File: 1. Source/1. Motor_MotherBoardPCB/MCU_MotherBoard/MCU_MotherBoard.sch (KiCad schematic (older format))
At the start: 0 parts

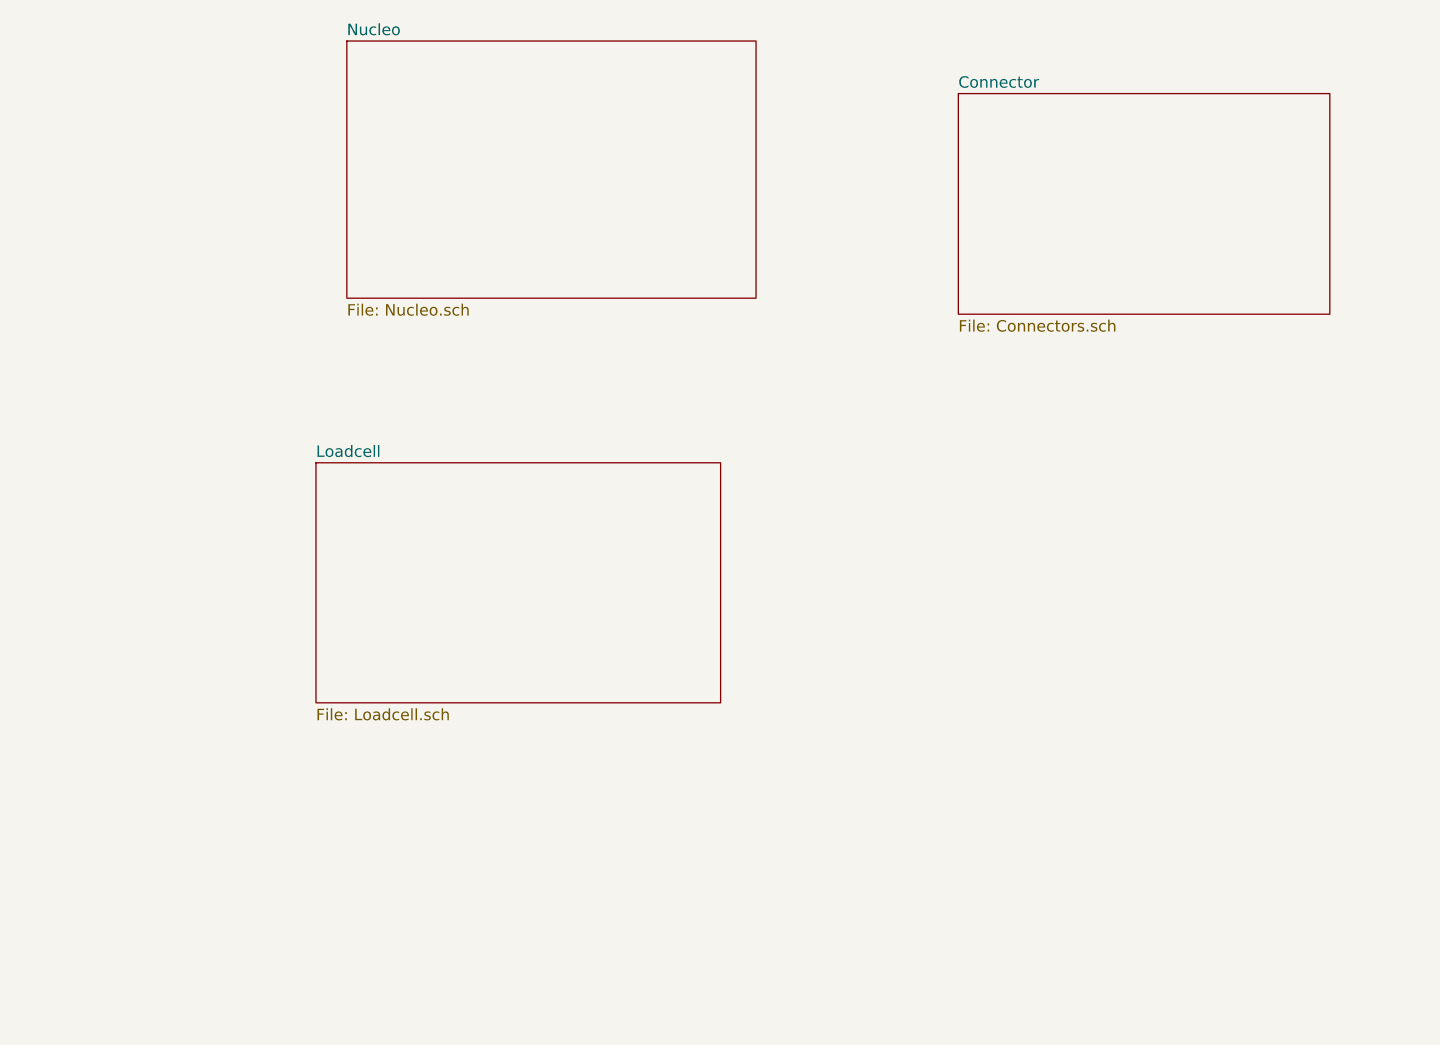
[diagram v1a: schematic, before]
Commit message: Add LoadCell_Click4 and SDCARD libraries
Add LoadCell_Click4 and SDCARD libraries
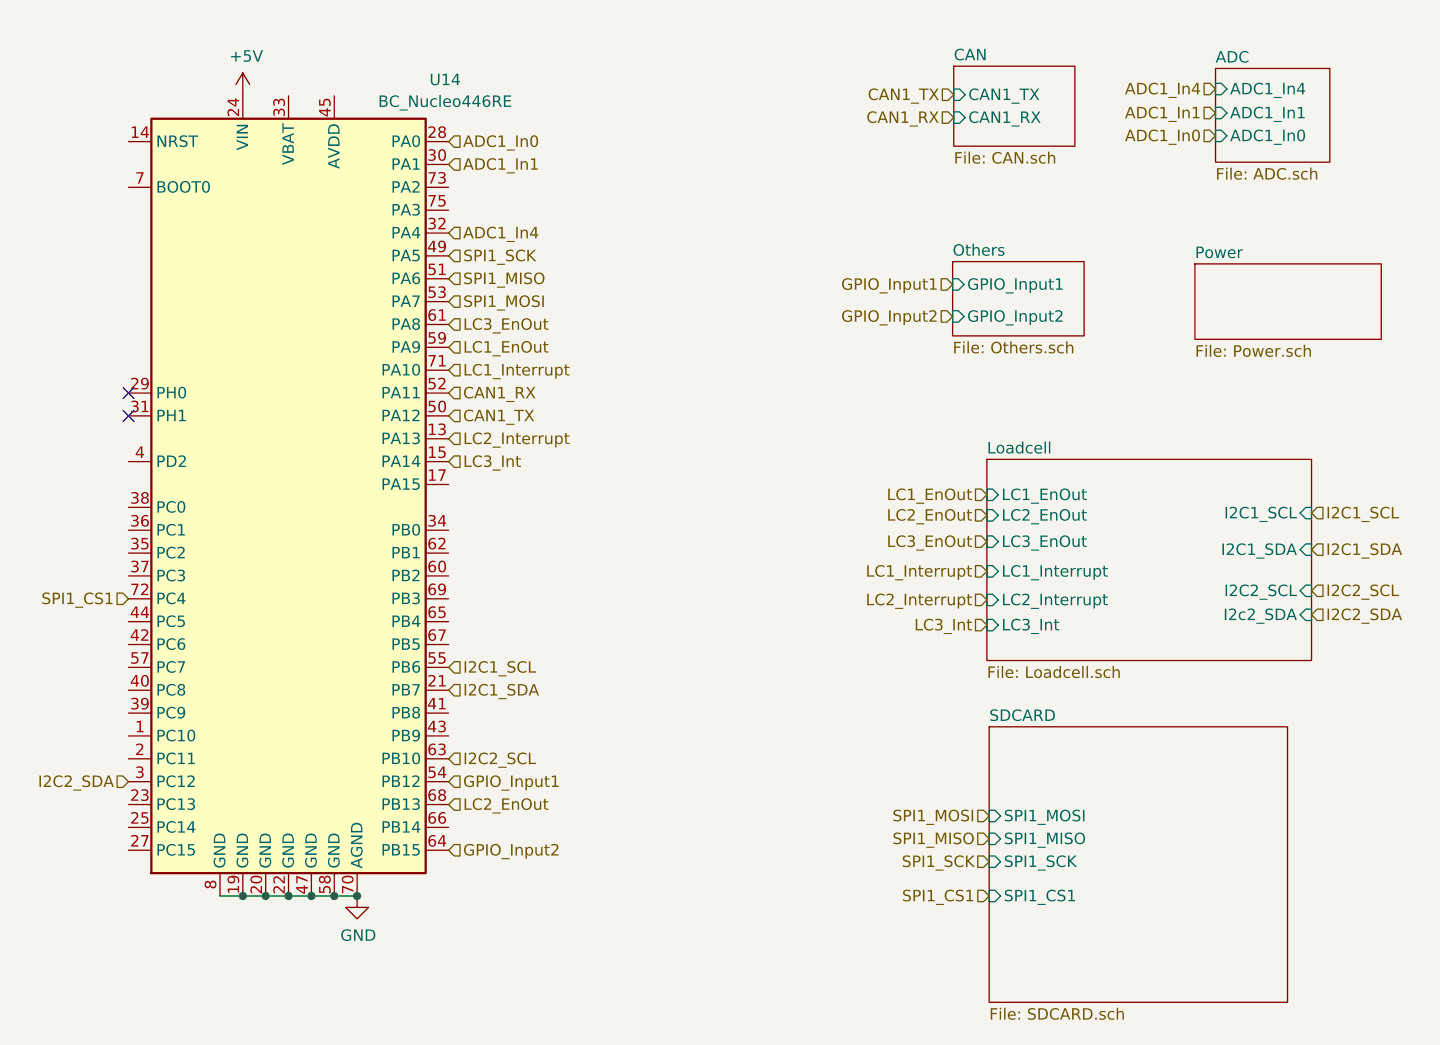
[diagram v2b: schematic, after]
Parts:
- added U14: BC_Nucleo446RE, BC_STM_Board:Main_NUCLEO-F446RE, symbol BC_Nucleo_boards:BC_Nucleo446RE
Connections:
- new net +5V: U14.24 (VIN)
- new net ADC1_In0: U14.28 (PA0)
- new net ADC1_In1: U14.30 (PA1)
- new net ADC1_In4: U14.32 (PA4)
- new net CAN1_RX: U14.52 (PA11)
- new net CAN1_TX: U14.50 (PA12)
- new net GND: U14.19 (GND), U14.20 (GND), U14.22 (GND), U14.47 (GND), U14.58 (GND), U14.70 (AGND), U14.8 (GND)
- new net GPIO_Input1: U14.54 (PB12)
- new net GPIO_Input2: U14.64 (PB15)
- new net I2C1_SCL: U14.55 (PB6)
- new net I2C1_SDA: U14.21 (PB7)
- new net I2C2_SCL: U14.63 (PB10)
- new net I2C2_SDA: U14.3 (PC12)
- new net LC1_EnOut: U14.59 (PA9)
- new net LC1_Interrupt: U14.71 (PA10)
- new net LC2_EnOut: U14.68 (PB13)
- new net LC2_Interrupt: U14.13 (PA13)
- new net LC3_EnOut: U14.61 (PA8)
- new net LC3_Int: U14.15 (PA14)
- new net SPI1_CS1: U14.72 (PC4)
- new net SPI1_MISO: U14.51 (PA6)
- new net SPI1_MOSI: U14.53 (PA7)
- new net SPI1_SCK: U14.49 (PA5)
- no-connect marks 0 -> 2
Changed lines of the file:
@@
 $Descr A4 11693 8268
 encoding utf-8
-Sheet 1 4
+Sheet 1 7
 Title ""
 Date ""
@@
 Comment4 ""
 $EndDescr
-$Sheet
-S 2095 1965 1790 1125
-U 6360BD6F
-F0 "Nucleo" 50
-F1 "Nucleo.sch" 50
-$EndSheet
-$Sheet
-S 4770 2195 1625 965
-U 6360BDB0
-F0 "Connector" 50
-F1 "Connectors.sch" 50
-$EndSheet
-$Sheet
-S 1960 3810 1770 1050
+$Comp
+L BC_Nucleo_boards:BC_Nucleo446RE U?
+U 1 1 63862899
+P 1840 3905
+AR Path="/6360BD6F/63862899" Ref="U?"  Part="1"
+AR Path="/63862899" Ref="U14"  Part="1"
+F 0 "U14" H 2525 5675 50  0000 C CNN
+F 1 "BC_Nucleo446RE" H 2525 5580 50  0000 C CNN
+F 2 "BC_STM_Board:Main_NUCLEO-F446RE" H 1240 2205 50  0001 R CNN
+F 3 "http://www.st.com/st-web-ui/static/active/en/resource/technical/document/datasheet/DM00141306.pdf" H 1840 3905 50  0001 C CNN
+	1    1840 3905
+	1    0    0    -1
+$EndComp
+Text HLabel 2540 4805 2    50   Input ~ 0
+I2C1_SDA
+Text HLabel 2540 4705 2    50   Input ~ 0
+I2C1_SCL
+NoConn ~ 1140 3505
+NoConn ~ 1140 3605
+Text HLabel 2540 3505 2    50   Input ~ 0
+CAN1_RX
+Text HLabel 2540 3605 2    50   Input ~ 0
+CAN1_TX
+Text HLabel 2540 5305 2    50   Input ~ 0
+LC2_EnOut
+Text HLabel 2540 3405 2    50   Input ~ 0
+LC1_Interrupt
+Wire Wire Line
+	1540 5705 1640 5705
+Connection ~ 1640 5705
+Wire Wire Line
+	1640 5705 1740 5705
+Connection ~ 1740 5705
+Wire Wire Line
+	1740 5705 1840 5705
+Connection ~ 1840 5705
+Wire Wire Line
+	1840 5705 1940 5705
+Connection ~ 1940 5705
+Wire Wire Line
+	1940 5705 2040 5705
+Connection ~ 2040 5705
+Wire Wire Line
+	2040 5705 2140 5705
+$Comp
+L power:GND #PWR?
+U 1 1 638628B2
+P 2140 5705
+AR Path="/6360BD6F/638628B2" Ref="#PWR?"  Part="1"
+AR Path="/638628B2" Ref="#PWR02"  Part="1"
+F 0 "#PWR02" H 2140 5455 50  0001 C CNN
+F 1 "GND" H 2145 5532 50  0000 C CNN
+F 2 "" H 2140 5705 50  0001 C CNN
+F 3 "" H 2140 5705 50  0001 C CNN
+	1    2140 5705
+	1    0    0    -1
+$EndComp
+Connection ~ 2140 5705
+$Comp
+L power:+5V #PWR?
+U 1 1 638628B9
+P 1640 2205
+AR Path="/6360BD6F/638628B9" Ref="#PWR?"  Part="1"
+AR Path="/638628B9" Ref="#PWR01"  Part="1"
+F 0 "#PWR01" H 1640 2055 50  0001 C CNN
+F 1 "+5V" H 1655 2378 50  0000 C CNN
+F 2 "" H 1640 2205 50  0001 C CNN
+F 3 "" H 1640 2205 50  0001 C CNN
+	1    1640 2205
+	1    0    0    -1
+$EndComp
+Text HLabel 2540 3305 2    50   Input ~ 0
+LC1_EnOut
+Text HLabel 2540 5105 2    50   Input ~ 0
+I2C2_SCL
+Text HLabel 2540 2905 2    50   Input ~ 0
+SPI1_SCK
+Text HLabel 2540 3005 2    50   Input ~ 0
+SPI1_MISO
+Text HLabel 2540 3105 2    50   Input ~ 0
+SPI1_MOSI
+Text HLabel 2540 5205 2    50   Input ~ 0
+GPIO_Input1
+Text HLabel 2540 5505 2    50   Input ~ 0
+GPIO_Input2
+Text HLabel 2540 2405 2    50   Input ~ 0
+ADC1_In0
+Text HLabel 2540 2805 2    50   Input ~ 0
+ADC1_In4
+Text HLabel 2540 2505 2    50   Input ~ 0
+ADC1_In1
+Text HLabel 1140 4405 0    50   Input ~ 0
+SPI1_CS1
+Text HLabel 1140 5205 0    50   Input ~ 0
+I2C2_SDA
+$Sheet
+S 4895 3795 1420 880
 U 6360BDDC
 F0 "Loadcell" 50
 F1 "Loadcell.sch" 50
-$EndSheet
+F2 "LC3_EnOut" I L 4895 4155 50
+F3 "LC2_EnOut" I L 4895 4040 50
+F4 "LC1_EnOut" I L 4895 3950 50
+F5 "LC1_Interrupt" I L 4895 4285 50
+F6 "LC2_Interrupt" I L 4895 4410 50
+F7 "LC3_Int" I L 4895 4520 50
+F8 "I2C1_SCL" I R 6315 4030 50
+F9 "I2C1_SDA" I R 6315 4190 50
+F10 "I2C2_SCL" I R 6315 4370 50
+F11 "I2c2_SDA" I R 6315 4475 50
+$EndSheet
+$Sheet
+S 4745 2930 575  325
+U 6360BDB0
+F0 "Others" 50
+F1 "Others.sch" 50
+F2 "GPIO_Input1" I L 4745 3030 50
+F3 "GPIO_Input2" I L 4745 3170 50
+$EndSheet
+Text HLabel 2540 3705 2    50   Input ~ 0
+LC2_Interrupt
+Text HLabel 2540 3805 2    50   Input ~ 0
+LC3_Int
+Text HLabel 2540 3205 2    50   Input ~ 0
+LC3_EnOut
+Text HLabel 4895 4155 0    50   Input ~ 0
+LC3_EnOut
+Text HLabel 4895 4040 0    50   Input ~ 0
+LC2_EnOut
+Text HLabel 4895 3950 0    50   Input ~ 0
+LC1_EnOut
+Text HLabel 4895 4285 0    50   Input ~ 0
+LC1_Interrupt
+Text HLabel 4895 4410 0    50   Input ~ 0
+LC2_Interrupt
+Text HLabel 4895 4520 0    50   Input ~ 0
+LC3_Int
+Text HLabel 6315 4190 2    50   Input ~ 0
+I2C1_SDA
+Text HLabel 6315 4030 2    50   Input ~ 0
+I2C1_SCL
+Text HLabel 6315 4475 2    50   Input ~ 0
+I2C2_SDA
+Text HLabel 6315 4370 2    50   Input ~ 0
+I2C2_SCL
+$Sheet
+S 4905 4965 1305 1205
+U 6386AD05
+F0 "SDCARD" 50
+F1 "SDCARD.sch" 50
+F2 "SPI1_MOSI" I L 4905 5355 50
+F3 "SPI1_MISO" I L 4905 5455 50
+F4 "SPI1_SCK" I L 4905 5555 50
+F5 "SPI1_CS1" I L 4905 5705 50
+$EndSheet
+$Sheet
+S 4750 2075 530  350
+U 6386E3EE
+F0 "CAN" 50
+F1 "CAN.sch" 50
+F2 "CAN1_TX" I L 4750 2200 50
+F3 "CAN1_RX" I L 4750 2300 50
+$EndSheet
+$Sheet
+S 5805 2940 815  330
+U 6386EE9C
+F0 "Power" 50
+F1 "Power.sch" 50
+$EndSheet
+$Sheet
+S 5895 2085 500  410
+U 6386F0B7
+F0 "ADC" 50
+F1 "ADC.sch" 50
+F2 "ADC1_In4" I L 5895 2175 50
+F3 "ADC1_In1" I L 5895 2280 50
+F4 "ADC1_In0" I L 5895 2380 50
+$EndSheet
+Text HLabel 4905 5555 0    50   Input ~ 0
+SPI1_SCK
+Text HLabel 4905 5455 0    50   Input ~ 0
+SPI1_MISO
+Text HLabel 4905 5355 0    50   Input ~ 0
+SPI1_MOSI
+Text HLabel 4905 5705 0    50   Input ~ 0
+SPI1_CS1
+Text HLabel 4750 2300 0    50   Input ~ 0
+CAN1_RX
+Text HLabel 4750 2200 0    50   Input ~ 0
+CAN1_TX
+Text HLabel 5895 2380 0    50   Input ~ 0
+ADC1_In0
+Text HLabel 5895 2175 0    50   Input ~ 0
+ADC1_In4
+Text HLabel 5895 2280 0    50   Input ~ 0
+ADC1_In1
+Text HLabel 4745 3030 0    50   Input ~ 0
+GPIO_Input1
+Text HLabel 4745 3170 0    50   Input ~ 0
+GPIO_Input2
 $EndSCHEMATC
